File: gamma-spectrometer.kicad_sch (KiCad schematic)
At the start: 45 parts, among them J1 *, J2 *, Q1 2N7002, U1 Pico 2, U3 TLV3201AIDBVR, U4 OPA357AIDBVR, U5 OPA357AIDBVR, U6 LM4040AIM3-3.0+T, U8 MAX5026EUT_T

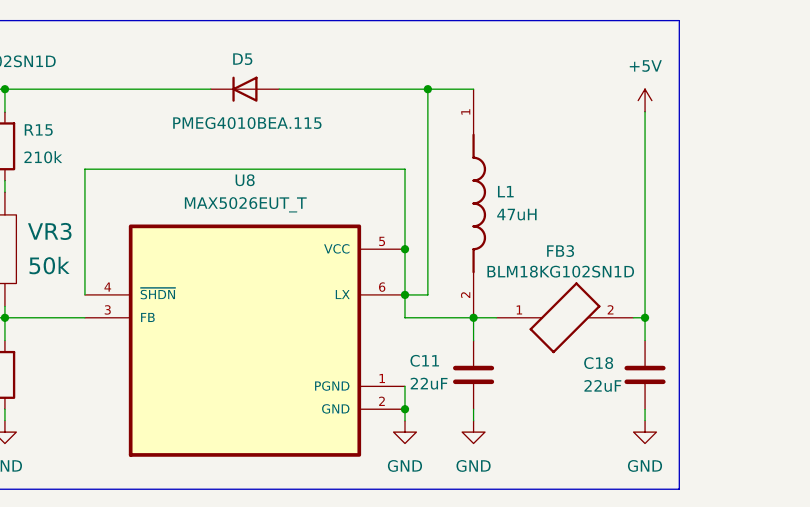
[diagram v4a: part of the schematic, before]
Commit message: Important fix for SiPM power supply circuit. Moved gerber files.
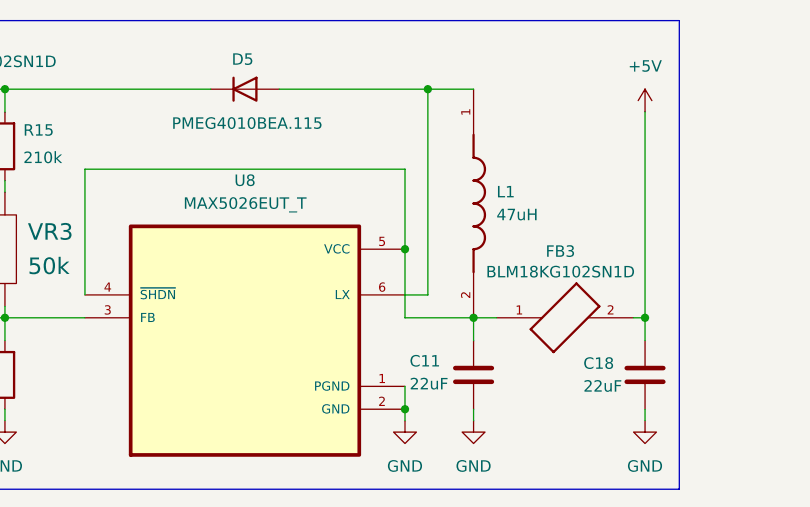
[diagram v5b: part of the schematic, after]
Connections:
- net at C11.1, FB3.1, L1.2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: no longer D5.2 (A), L1.1, U8.6 (LX)
- new net: D5.2 (A), L1.1, U8.6 (LX)
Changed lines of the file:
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@@
-	)
-	(junction
-		(at 130.81 170.18)
-		(diameter 0)
-		(color 0 0 0 0)
 	)
 	(junction
@@
 	(wire
 		(pts
-			(xy 130.81 165.1) (xy 130.81 170.18)
+			(xy 130.81 165.1) (xy 130.81 172.72)
 		)
 		(stroke
@@
 		)
 		(stroke
-			(width 0)
-			(type default)
-		)
-	)
-	(wire
-		(pts
-			(xy 130.81 170.18) (xy 130.81 172.72)
-		)
-		(stroke

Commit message: Updated BOM, schematic , foortprints, symbols
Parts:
- R10, R16: footprint ERJ3EKF2103V:RES_ERJ3EKF2103V -> ERJ3EKF1000V:RES_ERJ3EKF1000V
- R11, R14: footprint ERJ3EKF2103V:RES_ERJ3EKF2103V -> ERJ3EKF1002V:RES_ERJ3EKF1002V
- R12, R13, R8: footprint ERJ3EKF2103V:RES_ERJ3EKF2103V -> ERJ3EKF1001V:RES_ERJ3EKF1001V
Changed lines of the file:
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@@
 		(title "Gamma Spectrometer")
 		(date "2025-01-17")
-		(rev "0.1.1")
+		(rev "0.1.2")
 		(company "Vadym Vikulin")
 	)
@@
 			)
 		)
-		(property "Footprint" "ERJ3EKF2103V:RES_ERJ3EKF2103V"
+		(property "Footprint" "ERJ3EKF1001V:RES_ERJ3EKF1001V"
 			(at 35.56 103.632 90)
 			(effects
@@
 			)
 		)
-		(property "Footprint" "ERJ3EKF2103V:RES_ERJ3EKF2103V"
+		(property "Footprint" "ERJ3EKF1000V:RES_ERJ3EKF1000V"
 			(at 55.88 149.098 90)
 			(effects
@@
 			)
 		)
-		(property "Footprint" "ERJ3EKF2103V:RES_ERJ3EKF2103V"
+		(property "Footprint" "ERJ3EKF1001V:RES_ERJ3EKF1001V"
 			(at 196.088 31.75 90)
 			(effects
@@
 			)
 		)
-		(property "Footprint" "ERJ3EKF2103V:RES_ERJ3EKF2103V"
+		(property "Footprint" "ERJ3EKF1001V:RES_ERJ3EKF1001V"
 			(at 216.408 134.62 90)
 			(effects
@@
 			)
 		)
+		(property "Field5" ""
+			(at 214.63 134.62 0)
+			(effects
+				(font
+					(size 1.27 1.27)
+				)
+				(hide yes)
+			)
+		)
 		(pin "2"
 		)
@@
 			)
 		)
-		(property "Footprint" "ERJ3EKF2103V:RES_ERJ3EKF2103V"
+		(property "Footprint" "ERJ3EKF1002V:RES_ERJ3EKF1002V"
 			(at 227.33 76.708 90)
 			(effects
@@
 			)
 		)
-		(property "Footprint" "ERJ3EKF2103V:RES_ERJ3EKF2103V"
+		(property "Footprint" "ERJ3EKF1000V:RES_ERJ3EKF1000V"
 			(at 227.33 48.768 90)
 			(effects
@@
 			)
 		)
-		(property "Footprint" "ERJ3EKF2103V:RES_ERJ3EKF2103V"
+		(property "Footprint" "ERJ3EKF1002V:RES_ERJ3EKF1002V"
 			(at 88.138 179.07 90)
 			(effects
